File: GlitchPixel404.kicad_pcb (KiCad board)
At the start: 2 copper layers, 50 x 34 mm, 82 parts, among them J1 Barrel_Jack_Switch, J2 USB_C_Receptacle_USB2.0_16P, J3 VOLTLINK, J4 Conn_01x03, J5 Output, Q1 AONR21357-ES, Q2 MMBT3904, SW1 Reset, SW2 Boot, SW3 SW_SP3T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

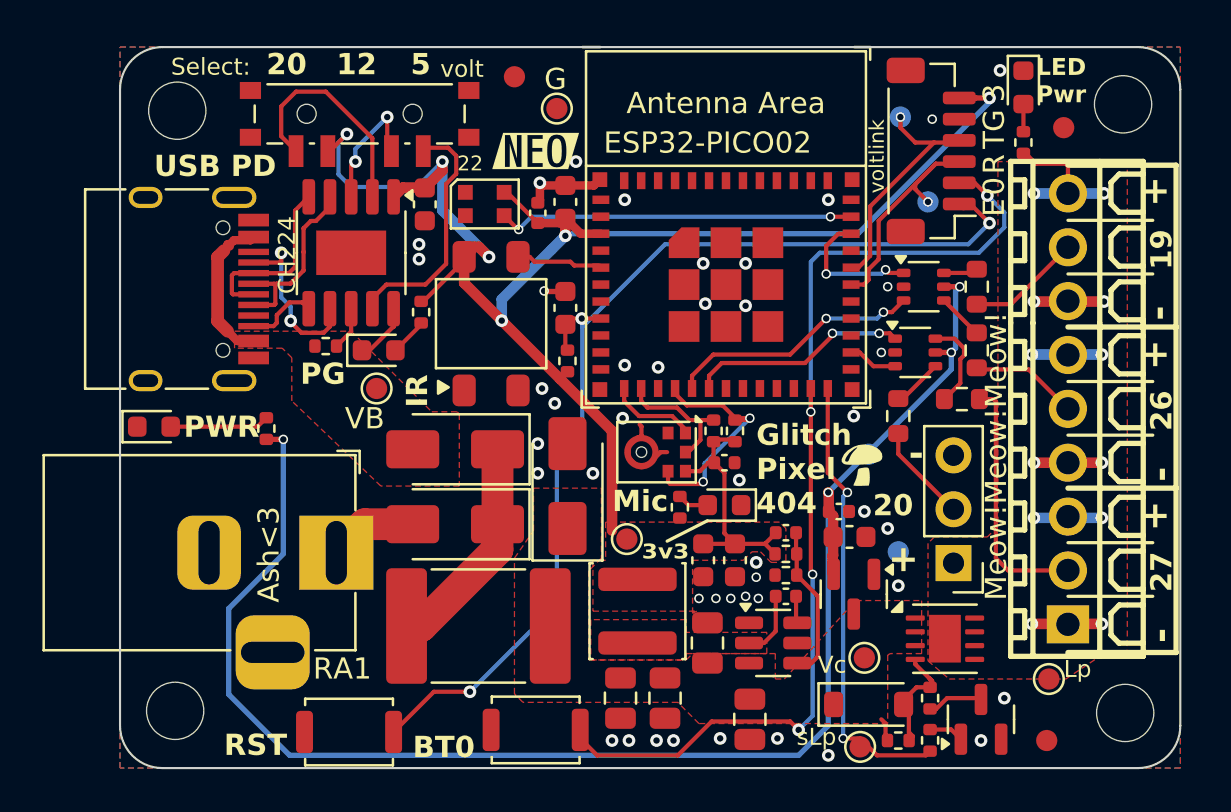
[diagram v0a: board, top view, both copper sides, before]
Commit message: Started A2 HW Rev, Fixed R12
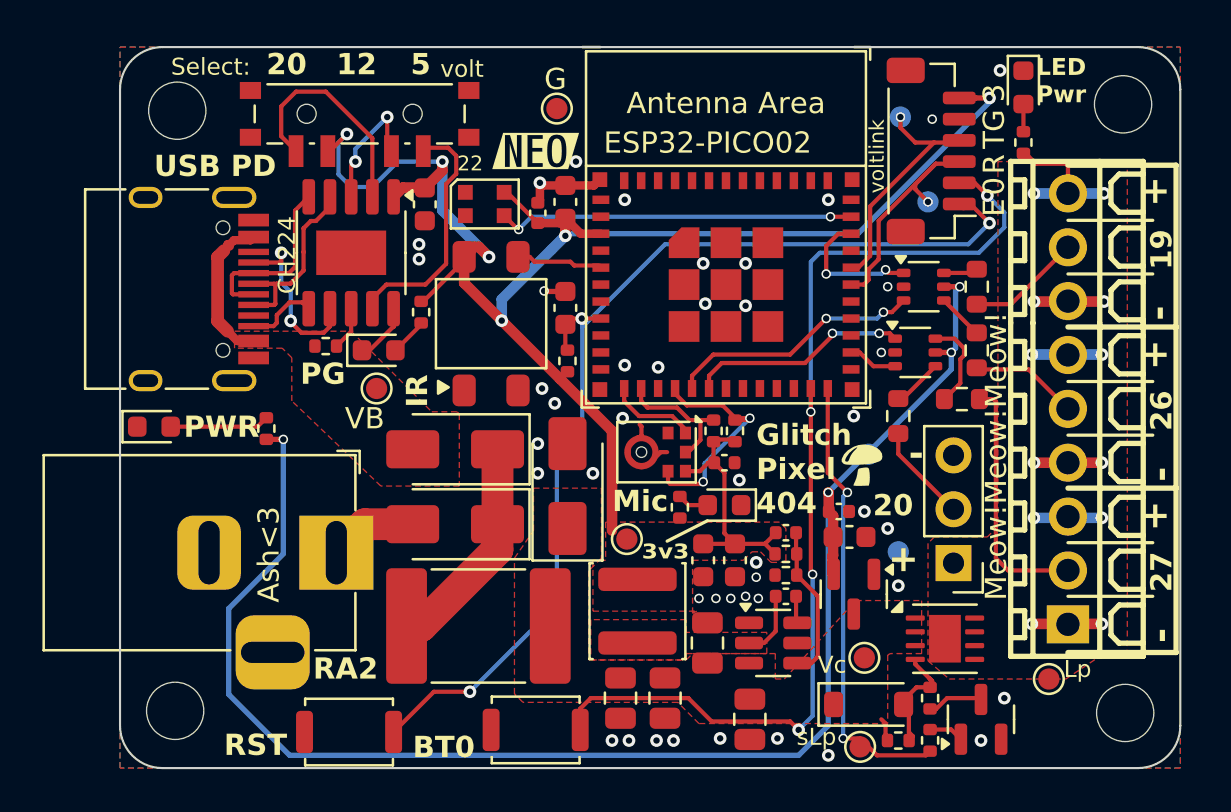
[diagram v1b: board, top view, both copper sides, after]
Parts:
- removed FID1, FID2, FID3: Fiducial, Fiducial:Fiducial_1mm_Mask2mm
- J2: value USB_C_Receptacle_USB2.0_16P -> TYPE-C-31-M-12
- R12: value 1k -> 10k
- renumbered U2 to Ue1
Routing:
- net /IO0: track 48.0 -> 49.1 mm
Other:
- board text added: "RA2"
- board text added: "RevA2"
- board text removed: "RA1"
- board text removed: "RevA1"

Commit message: Update silkscreen
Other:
- board text added: "05"
- board text removed: "5"
